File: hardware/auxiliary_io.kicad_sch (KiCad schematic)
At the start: 7 parts

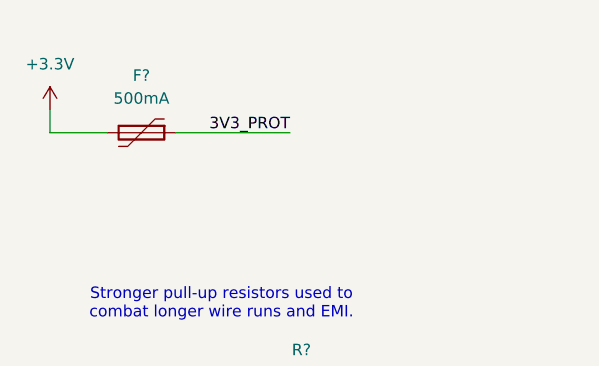
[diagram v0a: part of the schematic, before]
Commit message: Limit Switches and CAN Bus
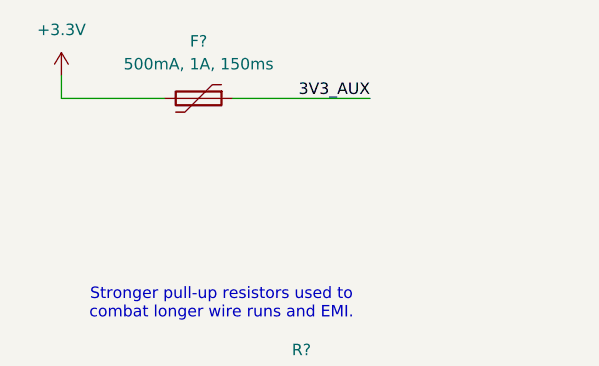
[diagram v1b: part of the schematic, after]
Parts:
- removed F?: 500mA, symbol Device:Polyfuse
- added F?: 500mA, 1A, 150ms, Fuse:Fuse_1812_4532Metric, symbol Device:Polyfuse
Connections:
- net +3.3V: now also F?.2
- new net 3V3_AUX: F?.1
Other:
- company: (none) -> Jacob Wigent
- title: (none) -> Auxiliary IO
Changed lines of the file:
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@@
 	(generator "eeschema")
 	(generator_version "10.0")
-	(paper "A4")
+	(paper "A")
+	(title_block
+		(title "Auxiliary IO")
+		(rev "A")
+		(company "Jacob Wigent")
+	)
 	(text "Stronger pull-up resistors used to\ncombat longer wire runs and EMI."
 		(exclude_from_sim no)
@@
 	(wire
 		(pts
-			(xy 63.5 31.75) (xy 69.85 31.75)
+			(xy 83.82 27.94) (xy 99.06 27.94)
 		)
 		(stroke
@@
 	(wire
 		(pts
-			(xy 111.76 66.04) (xy 114.3 66.04)
+			(xy 64.77 25.4) (xy 64.77 27.94)
 		)
 		(stroke
@@
 	(wire
 		(pts
-			(xy 104.14 73.66) (xy 114.3 73.66)
+			(xy 111.76 66.04) (xy 114.3 66.04)
 		)
 		(stroke
@@
 	(wire
 		(pts
-			(xy 63.5 29.21) (xy 63.5 31.75)
+			(xy 104.14 73.66) (xy 114.3 73.66)
 		)
 		(stroke
@@
 	(wire
 		(pts
-			(xy 104.14 71.12) (xy 114.3 71.12)
+			(xy 64.77 27.94) (xy 76.2 27.94)
 		)
 		(stroke
@@
 	(wire
 		(pts
-			(xy 77.47 31.75) (xy 90.17 31.75)
+			(xy 104.14 71.12) (xy 114.3 71.12)
 		)
 		(stroke
@@
 		)
 	)
-	(label "3V3_PROT"
-		(at 90.17 31.75 180)
+	(label "3V3_AUX"
+		(at 99.06 27.94 180)
 		(effects
 			(font
@@
 	)
 	(symbol
-		(lib_id "Device:Polyfuse")
-		(at 73.66 31.75 270)
-		(unit 1)
-		(body_style 1)
-		(exclude_from_sim no)
-		(in_bom yes)
-		(on_board yes)
-		(in_pos_files yes)
-		(dnp no)
-		(fields_autoplaced yes)
-		(property "Reference" "F?"
-			(at 73.66 25.4 90)
-			(show_name no)
-			(do_not_autoplace no)
-			(effects
-				(font
-					(size 1.27 1.27)
-				)
-			)
-		)
-		(property "Value" "500mA"
-			(at 73.66 27.94 90)
-			(show_name no)
-			(do_not_autoplace no)
-			(effects
-				(font
-					(size 1.27 1.27)
-				)
-			)
-		)
-		(property "Footprint" ""
-			(at 68.58 33.02 0)
-			(hide yes)
-			(show_name no)
-			(do_not_autoplace no)
-			(effects
-				(font
-					(size 1.27 1.27)
-				)
-				(justify left)
-			)
-		)
-		(property "Datasheet" ""
-			(at 73.66 31.75 0)
-			(hide yes)
-			(show_name no)
-			(do_not_autoplace no)
-			(effects
-				(font
-					(size 1.27 1.27)
-				)
-			)
-		)
-		(property "Description" "Resettable fuse, polymeric positive temperature coefficient"
-			(at 73.66 31.75 0)
-			(hide yes)
-			(show_name no)
-			(do_not_autoplace no)
-			(effects
-				(font
-					(size 1.27 1.27)
-				)
-			)
-		)
-		(pin "2"
-		)
-		(pin "1"
-		)
-		(instances
-			(project "stepping-stone"
-				(path "/793a882e-3f7b-468b-a863-41a1f527e1bf/4251703e-8697-4078-b9d0-81c0cbfbf2bf"
-					(reference "F?")
-					(unit 1)
-				)
-			)
-		)
-	)
-	(symbol
 		(lib_id "Device:R_US")
 		(at 91.44 60.96 90)
@@
 	)
 	(symbol
-		(lib_id "power:+3.3V")
-		(at 63.5 29.21 0)
+		(lib_id "Device:R_US")
+		(at 100.33 71.12 90)
+		(mirror x)
 		(unit 1)
 		(body_style 1)
@@
 		(in_pos_files yes)
 		(dnp no)
-		(fields_autoplaced yes)
-		(property "Reference" "#PWR0206"
-			(at 63.5 33.02 0)
-			(hide yes)
+		(property "Reference" "R?"
+			(at 100.33 66.04 90)
 			(show_name no)
 			(do_not_autoplace no)
@@
 			)
 		)
-		(property "Value" "+3.3V"
-			(at 63.5 24.13 0)
+		(property "Value" "100R"
+			(at 100.33 68.58 90)
 			(show_name no)
 			(do_not_autoplace no)
@@
 			)
 		)
-		(property "Footprint" ""
-			(at 63.5 29.21 0)
+		(property "Footprint" "Resistor_SMD:R_0603_1608Metric"
+			(at 100.584 72.136 90)
 			(hide yes)
 			(show_name no)
@@
 		)
 		(property "Datasheet" ""
-			(at 63.5 29.21 0)
+			(at 100.33 71.12 0)
 			(hide yes)
 			(show_name no)
@@
 			)
 		)
-		(property "Description" "Power symbol creates a global label with name \"+3.3V\""
-			(at 63.5 29.21 0)
+		(property "Description" "Resistor, US symbol"
+			(at 100.33 71.12 0)
+			(hide yes)
+			(show_name no)
+			(do_not_autoplace no)
+			(effects
+				(font
+					(size 1.27 1.27)
+				)
+			)
+		)
+		(property "Part Number" "RC0603FR-07100RL"
+			(at 100.33 71.12 0)
+			(hide yes)
+			(show_name no)
+			(do_not_autoplace no)
+			(effects
+				(font
+					(size 1.27 1.27)
+				)
+			)
+		)
+		(property "Vendor URL" "https://www.digikey.com/en/products/detail/yageo/RC0603FR-07100RL/726888"
+			(at 100.33 71.12 0)
 			(hide yes)
 			(show_name no)
@@
 		(pin "1"
 		)
+		(pin "2"
+		)
 		(instances
 			(project "stepping-stone"
 				(path "/793a882e-3f7b-468b-a863-41a1f527e1bf/4251703e-8697-4078-b9d0-81c0cbfbf2bf"
-					(reference "#PWR0206")
+					(reference "R?")
 					(unit 1)
 				)
@@
 	)
 	(symbol
-		(lib_id "Device:R_US")
-		(at 100.33 71.12 90)
-		(mirror x)
+		(lib_id "power:+3.3V")
+		(at 64.77 25.4 0)
 		(unit 1)
 		(body_style 1)
@@
 		(in_pos_files yes)
 		(dnp no)
-		(property "Reference" "R?"
-			(at 100.33 66.04 90)
-			(show_name no)
-			(do_not_autoplace no)
-			(effects
-				(font
-					(size 1.27 1.27)
-				)
-			)
-		)
-		(property "Value" "100R"
-			(at 100.33 68.58 90)
-			(show_name no)
-			(do_not_autoplace no)
-			(effects
-				(font
-					(size 1.27 1.27)
-				)
-			)
-		)
-		(property "Footprint" "Resistor_SMD:R_0603_1608Metric"
-			(at 100.584 72.136 90)
+		(fields_autoplaced yes)
+		(property "Reference" "#PWR0206"
+			(at 64.77 29.21 0)
 			(hide yes)
 			(show_name no)
@@
 			)
 		)
-		(property "Datasheet" ""
-			(at 100.33 71.12 0)
-			(hide yes)
+		(property "Value" "+3.3V"
+			(at 64.77 20.32 0)
 			(show_name no)
 			(do_not_autoplace no)
@@
 			)
 		)
-		(property "Description" "Resistor, US symbol"
-			(at 100.33 71.12 0)
+		(property "Footprint" ""
+			(at 64.77 25.4 0)
 			(hide yes)
 			(show_name no)
@@
 			)
 		)
-		(property "Part Number" "RC0603FR-07100RL"
-			(at 100.33 71.12 0)
+		(property "Datasheet" ""
+			(at 64.77 25.4 0)
 			(hide yes)
 			(show_name no)
@@
 			)
 		)
-		(property "Vendor URL" "https://www.digikey.com/en/products/detail/yageo/RC0603FR-07100RL/726888"
-			(at 100.33 71.12 0)
+		(property "Description" "Power symbol creates a global label with name \"+3.3V\""
+			(at 64.77 25.4 0)
 			(hide yes)
 			(show_name no)
@@
 		(pin "1"
 		)
-		(pin "2"
-		)
 		(instances
 			(project "stepping-stone"
 				(path "/793a882e-3f7b-468b-a863-41a1f527e1bf/4251703e-8697-4078-b9d0-81c0cbfbf2bf"
-					(reference "R?")
+					(reference "#PWR0206")
 					(unit 1)
 				)
@@
 					(unit 1)
 				)
+			)
+		)
+	)
+	(symbol
+		(lib_id "Device:Polyfuse")
+		(at 80.01 27.94 270)
+		(unit 1)
+		(body_style 1)
+		(exclude_from_sim no)
+		(in_bom yes)
+		(on_board yes)
+		(in_pos_files yes)
+		(dnp no)
+		(fields_autoplaced yes)
+		(property "Reference" "F?"
+			(at 80.01 21.59 90)
+			(show_name no)
+			(do_not_autoplace no)
+			(effects
+				(font
+					(size 1.27 1.27)
+				)
+			)
+		)
+		(property "Value" "500mA, 1A, 150ms"
+			(at 80.01 24.13 90)
+			(show_name no)
+			(do_not_autoplace no)
+			(effects
+				(font
+					(size 1.27 1.27)
+				)
+			)
+		)
+		(property "Footprint" "Fuse:Fuse_1812_4532Metric"
+			(at 74.93 29.21 0)
+			(hide yes)
+			(show_name no)
+			(do_not_autoplace no)
+			(effects
+				(font
+					(size 1.27 1.27)
+				)
+				(justify left)
+			)
+		)
+		(property "Datasheet" "https://www.belfuse.com/media/datasheets/products/circuit-protection/ds-cp-0zcm-series.pdf"
+			(at 80.01 27.94 0)
+			(hide yes)
+			(show_name no)
+			(do_not_autoplace no)
+			(effects
+				(font
+					(size 1.27 1.27)
+				)
+			)
+		)
+		(property "Description" "Resettable fuse, polymeric positive temperature coefficient"
+			(at 80.01 27.94 0)
+			(hide yes)
+			(show_name no)
+			(do_not_autoplace no)
+			(effects
+				(font
+					(size 1.27 1.27)
+				)
+			)
+		)
+		(property "Part Number" "0ZCG0050AF2C"
+			(at 80.01 27.94 0)
+			(hide yes)
+			(show_name no)
+			(do_not_autoplace no)
+			(effects
+				(font
+					(size 1.27 1.27)
+				)
+			)
+		)
+		(property "Vendor URL" "https://www.digikey.com/en/products/detail/bel-fuse-inc/0ZCG0050AF2C/4156100"
+			(at 80.01 27.94 0)
+			(hide yes)
+			(show_name no)
+			(do_not_autoplace no)
+			(effects
+				(font
+					(size 1.27 1.27)
+				)
+			)
+		)
+		(pin "2"
+		)
+		(pin "1"
+		)
+		(instances
+			(project "stepping-stone"
+				(path "/793a882e-3f7b-468b-a863-41a1f527e1bf/4251703e-8697-4078-b9d0-81c0cbfbf2bf"
+					(reference "F?")
+					(unit 1)
+				)

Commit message: Finish aux i2c, uart, gpio
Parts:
- removed R? (x2): 100R, Resistor_SMD:R_0603_1608Metric, symbol Device:R_US
- removed R?: 2.2k, Resistor_SMD:R_0603_1608Metric, symbol Device:R_US
- added D? (x6): ESD9B3.3ST5G, Diode_SMD:D_SOD-923, symbol Diode:SMAJ28A
- added J?: UART, symbol Connector_Generic:Conn_01x04
- added J?: GPIO, symbol Connector_Generic:Conn_01x06
- added J?: I2C_B, symbol Connector_Generic:Conn_01x04
- added R? (x9): 10k, Resistor_SMD:R_0603_1608Metric, symbol Device:R_US
- added R? (x8): 100R, Resistor_SMD:R_0603_1608Metric, symbol Device:R_US
- added R?: 2.2k, Resistor_SMD:R_0603_1608Metric, symbol Device:R_US
- J?: value Conn_01x04 -> I2C_A
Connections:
- net +3.3V: now also R?.2, R?.1, R?.1, R?.1, R?.1, R?.1, R?.2
- net 3V3_AUX: now also J?.2 (Pin_2), D?.1 (A1), D?.1 (A1), J?.2 (Pin_2), J?.2 (Pin_2), J?.2 (Pin_2)
- net GND: now also D?.2 (A2), D?.2 (A2), D?.2 (A2), D?.2 (A2), D?.2 (A2), D?.2 (A2), J?.1 (Pin_1), J?.1 (Pin_1), J?.1 (Pin_1), R?.2, R?.2, R?.2, R?.2
- net SCL: now also R?.1
- net SDA: now also R?.1
- net at R?.1: now also J?.3 (Pin_3), D?.1 (A1), J?.3 (Pin_3), R?.2
- net at J?.4 (Pin_4): now also D?.1 (A1), J?.4 (Pin_4), R?.1, R?.2
- new net: J?.3 (Pin_3), R?.1, R?.2, R?.2
- new net: D?.1 (A1), J?.4 (Pin_4), R?.2, R?.2
- new net: J?.5 (Pin_5), R?.1, R?.2, R?.2
- new net: D?.1 (A1), J?.3 (Pin_3), R?.2
- new net: J?.4 (Pin_4), R?.1, R?.2, R?.2
- new net: J?.6 (Pin_6), R?.1, R?.2, R?.2
- new net GPIO_A: R?.1
- new net GPIO_B: R?.1
- new net GPIO_C: R?.1
- new net GPIO_D: R?.1
- new net RX: R?.1
- new net TX: R?.1
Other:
- note added: "ANALOG"
- note added: "Exposed ADC/DAC pins from MCU."
- note added: "Exposed general purpose IO pins from MCU."
- note added: "GPIO"
- note added: "I2C"
- note added: "Optional pull-down resistor pads."
- note added: "Optional pull-up resistor pads."
- note added: "Series resistors used for dampening and MCU protection."
- note added: "Shared ESD protection on bus to limit BOM and capacitance."
- note added: "Standard pull-up resistor to prevent floating RX."
- note added: "UART"
- note added: "Used for general communication off-board."
- note added: "Used to connect COTS sensors using STEMMA connector convention."
- note removed: "Series resistors used to limit current in case of external short."
- moved on the sheet: J?, R?

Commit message: Minor Changes
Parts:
- added D?: ESD9B3, Diode_SMD:D_SOD-923, symbol Diode:SMAJ28A
- added D? (x4): ESD9B3.3ST5G, Diode_SMD:D_SOD-923, symbol Diode:SMAJ28A
- D? (x2): value ESD9B3.3ST5G -> ESD9B3
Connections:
- net 3V3_AUX: now also D?.1 (A1)
- net GND: now also D?.2 (A2), D?.2 (A2), D?.2 (A2), D?.2 (A2), D?.2 (A2)
- net at J?.3 (Pin_3), R?.1, R?.2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: now also D?.1 (A1)
- net at J?.5 (Pin_5), R?.1, R?.2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: now also D?.1 (A1)
- net at J?.4 (Pin_4), R?.1, R?.2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: now also D?.1 (A1)
- net at J?.6 (Pin_6), R?.1, R?.2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: now also D?.1 (A1)
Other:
- moved on the sheet: R?

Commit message: Aux IO Changes
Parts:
- removed J?: GPIO, symbol Connector_Generic:Conn_01x06
- removed J?: Conn_01x03, symbol Connector_Generic:Conn_01x03
- added C? (x4): 0.1uF, Capacitor_SMD:C_0603_1608Metric_Pad1.08x0.95mm_HandSolder, symbol Device:C_Small
- added D?: ESD9B3, Diode_SMD:D_SOD-923, symbol Diode:SMAJ28A
- added D? (x3): ESD9B3.3ST5G, Diode_SMD:D_SOD-923, symbol Diode:SMAJ28A
- added J?: GPIO/AIO, Connector_PinHeader_2.54mm:PinHeader_2x05_P2.54mm_Vertical, symbol Connector_Generic:Conn_02x05_Odd_Even
- added R? (x4): 100R, Resistor_SMD:R_0603_1608Metric, symbol Device:R_US
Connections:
- net 3V3_AUX: now also J?.2 (Pin_2)
- net GND: now also C?.2, C?.2, C?.2, C?.2, D?.2 (A2), D?.2 (A2), D?.2 (A2), D?.2 (A2), J?.1 (Pin_1)
- net at D?.1 (A1), R?.1, R?.2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: now also J?.3 (Pin_3)
- net at D?.1 (A1), R?.1, R?.2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: now also J?.7 (Pin_7)
- net at D?.1 (A1), R?.1, R?.2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: now also J?.5 (Pin_5)
- net at D?.1 (A1), R?.1, R?.2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: now also J?.9 (Pin_9)
- new net: D?.1 (A1), J?.6 (Pin_6), R?.1
- new net: D?.1 (A1), J?.10 (Pin_10), R?.1
- new net: D?.1 (A1), J?.4 (Pin_4), R?.1
- new net: D?.1 (A1), J?.8 (Pin_8), R?.1
- new net AIO_A: C?.1, R?.2
- new net AIO_B: C?.1, R?.2
- new net AIO_C: C?.1, R?.2
- new net AIO_D: C?.1, R?.2
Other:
- note added: "Capacitors for ADC sampling stability."
- moved on the sheet: D?, F?, J?, R?
